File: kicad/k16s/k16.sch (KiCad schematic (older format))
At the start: 352 parts, among them J1 PCIEPWR, J3 PINHD-1X4, J5 PINHD-1X4, Q1 NDS351AN, U1 AVALON, U10 AVALON, U11 AVALON, U12 AVALON, U13 AVALON, U14 AVALON, U15 AVALON, U16 AVALON, U17 PIC16LF1459, U18 IR3895, U19 IR3895, U2 AVALON, U20 MCP16321, U21 NL27WZ14, U22 AP7217D / RT9166A, U23 AP7217D / RT9166A, U24 74AUP2G02, U25 NL27WZ14, U3 AVALON, U4 AVALON, U5 AVALON, U6 AVALON, U7 AVALON, U8 AVALON, U9 AVALON, X1 ASMDB

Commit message: update K1 to 0.3.0
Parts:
- R24, R25: value 2.2K -> 1K
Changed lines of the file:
@@
-EESchema Schematic File Version 2  date Mon 15 Jul 2013 02:06:03 PM ICT
+EESchema Schematic File Version 2  date Thu 18 Jul 2013 10:01:42 PM ICT
 LIBS:k16
 LIBS:power
@@
 Sheet 1 1
 Title "Klondike 16 ASIC Miner"
-Date "15 jul 2013"
+Date "18 jul 2013"
 Rev ""
 Comp ""
@@
 U 1 1 51835C6D
 P 13165 5915
-F 0 "R25" H 13117 5932 22  0000 L BNN
-F 1 "2.2K" H 13117 5873 22  0000 L BNN
+F 0 "R25" V 13072 5944 22  0000 L BNN
+F 1 "1K" V 13111 5941 22  0000 L BNN
 F 2 "" H 13165 5915 60  0001 C CNN
 F 3 "" H 13165 5915 60  0001 C CNN
@@
 U 1 1 51835C78
 P 13049 5913
-F 0 "R24" H 13001 5930 22  0000 L BNN
-F 1 "2.2K" H 13001 5871 22  0000 L BNN
+F 0 "R24" V 13001 5808 22  0000 L BNN
+F 1 "1K" V 13051 5809 22  0000 L BNN
 F 2 "" H 13049 5913 60  0001 C CNN
 F 3 "" H 13049 5913 60  0001 C CNN

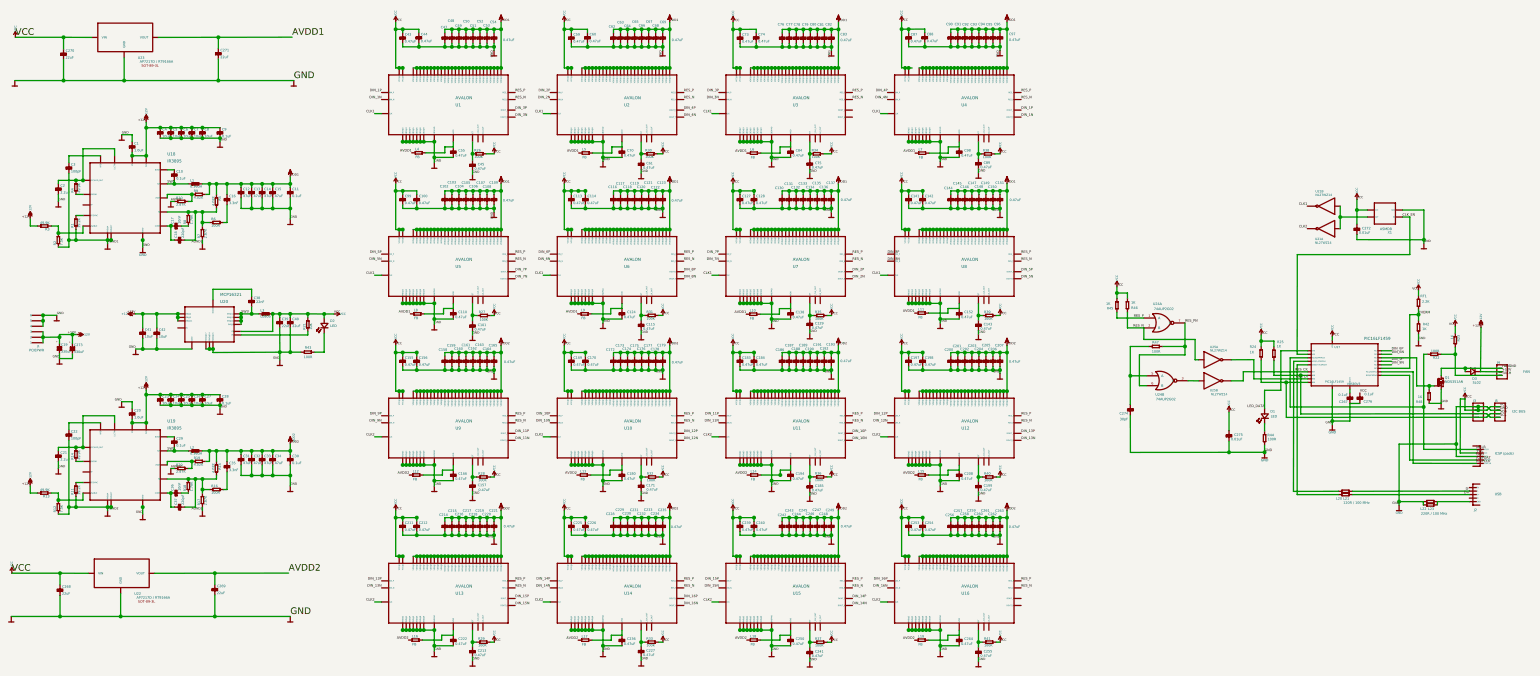
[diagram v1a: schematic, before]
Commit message: update firmware for 16 chips, add dist files
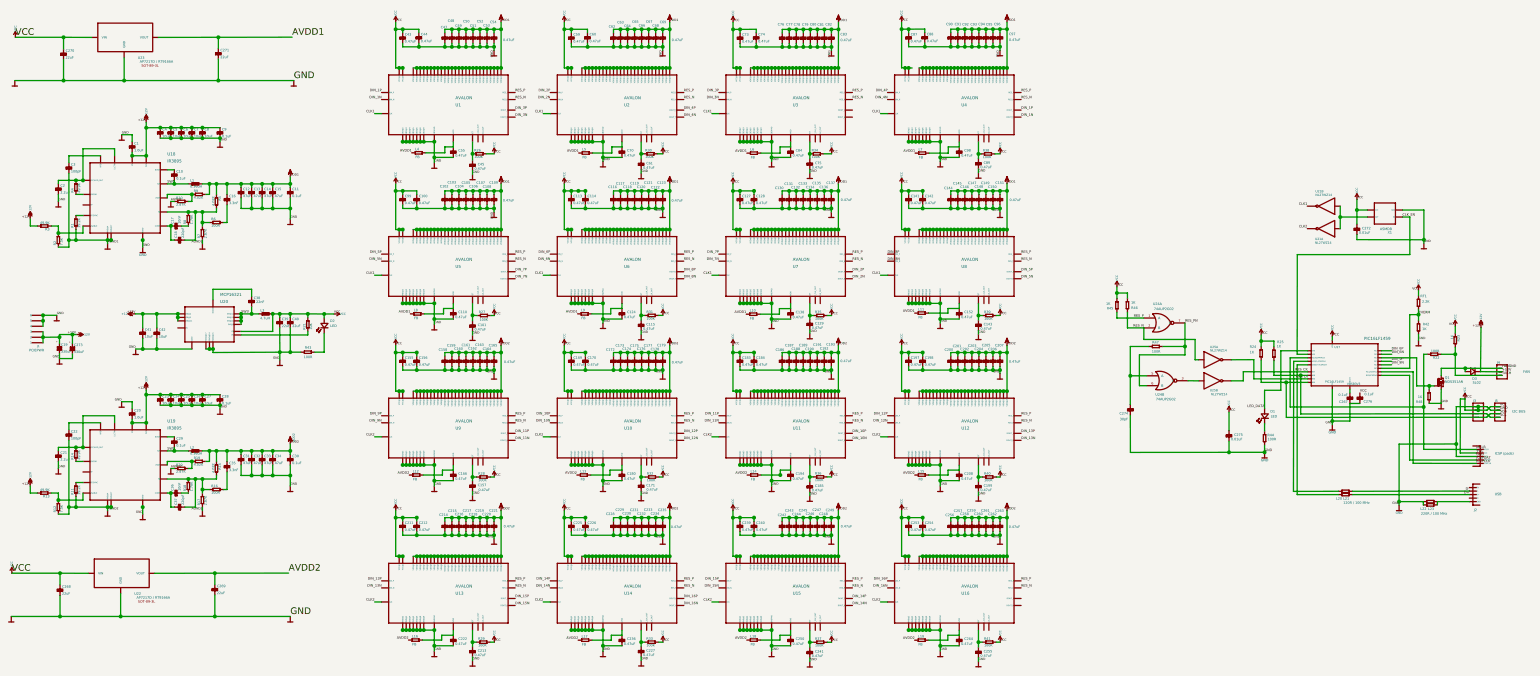
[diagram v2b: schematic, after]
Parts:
- L20: value 120R @ 100 MHz -> 120R / 100 MHz
- L22: value 120R @ 100 MHz -> 220R / 100 MHz
- L3: value L0805 -> 4.7uH
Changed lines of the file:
@@
-EESchema Schematic File Version 2  date Thu 18 Jul 2013 10:01:42 PM ICT
+EESchema Schematic File Version 2  date Mon 12 Aug 2013 08:32:43 AM ICT
 LIBS:k16
 LIBS:power
@@
 Sheet 1 1
 Title "Klondike 16 ASIC Miner"
-Date "18 jul 2013"
+Date "12 aug 2013"
 Rev ""
 Comp ""
@@
 P 3982 5553
 F 0 "L3" H 3934 5571 22  0000 L BNN
-F 1 "L0805" H 3934 5517 22  0000 L BNN
+F 1 "4.7uH" H 3932 5501 22  0000 L BNN
 F 2 "" H 3982 5553 60  0001 C CNN
 F 3 "" H 3982 5553 60  0001 C CNN
@@
 	15224 6398 15137 6398
 Wire Wire Line
-	15106 6430 15137 6398
+	15137 6398 15106 6430
 Wire Wire Line
 	15224 6430 15139 6431
 Wire Wire Line
-	15106 6398 15139 6431
+	15139 6431 15106 6398
 Wire Wire Line
-	14826 6398 15106 6398
+	15106 6398 14826 6398
 Wire Wire Line
-	14905 6430 15106 6430
+	15106 6430 14905 6430
 Connection ~ 15026 6398
 Connection ~ 15026 6430
@@
 	9199 2962 9199 2898
 Wire Wire Line
-	9199 2962 9198 3313
+	9198 3313 9199 2962
 Wire Wire Line
 	8687 2994 8687 2962
@@
 	11940 6207 11940 5926
 Wire Wire Line
-	12355 5927 11940 5926
+	11940 5926 12355 5927
 Wire Wire Line
-	12355 5636 12355 5927
+	12355 5927 12355 5636
 Wire Wire Line
 	11980 5786 12447 5786
@@
 P 13817 7169
 F 0 "L20" H 13730 7090 22  0000 L BNN
-F 1 "120R @ 100 MHz" H 13794 7198 22  0001 L BNN
+F 1 "120R / 100 MHz" H 13794 7198 22  0001 L BNN
 F 2 "" H 13817 7169 60  0001 C CNN
 F 3 "" H 13817 7169 60  0001 C CNN
@@
 P 14590 7263
 F 0 "L22" H 14499 7185 22  0000 L BNN
-F 1 "120R @ 100 MHz" H 14567 7292 22  0001 L BNN
+F 1 "220R / 100 MHz" H 14567 7292 22  0001 L BNN
 F 2 "" H 14590 7263 60  0001 C CNN
 F 3 "" H 14590 7263 60  0001 C CNN
